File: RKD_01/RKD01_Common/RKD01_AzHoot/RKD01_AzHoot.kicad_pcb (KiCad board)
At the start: 2 copper layers, 19.1 x 28.6 mm, 3 parts, among them M1 Mark, P1 pointing

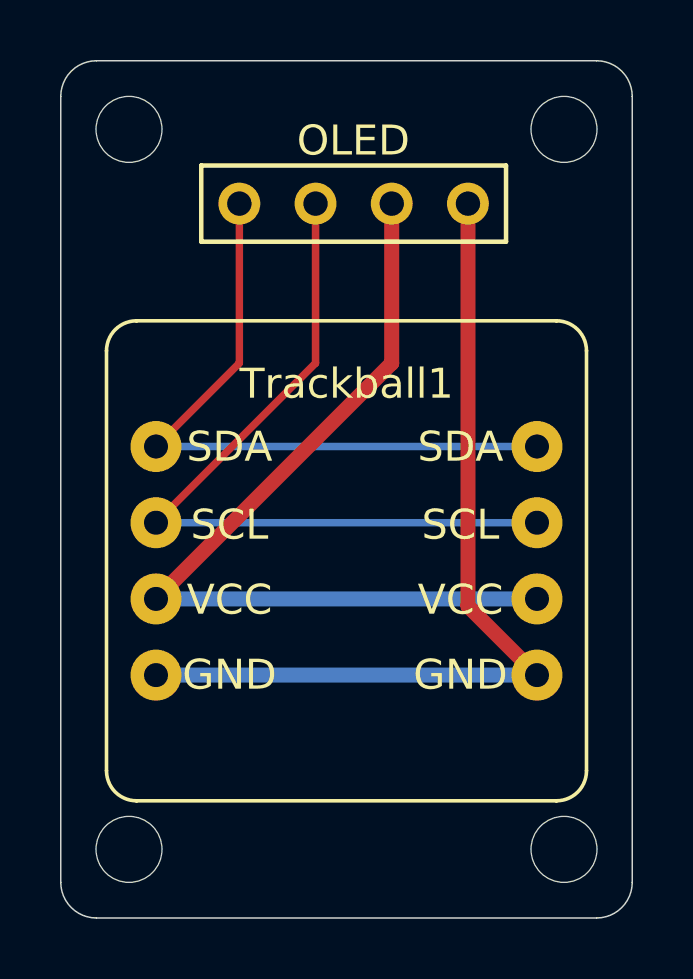
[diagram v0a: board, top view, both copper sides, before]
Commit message: 足場をカットに更新
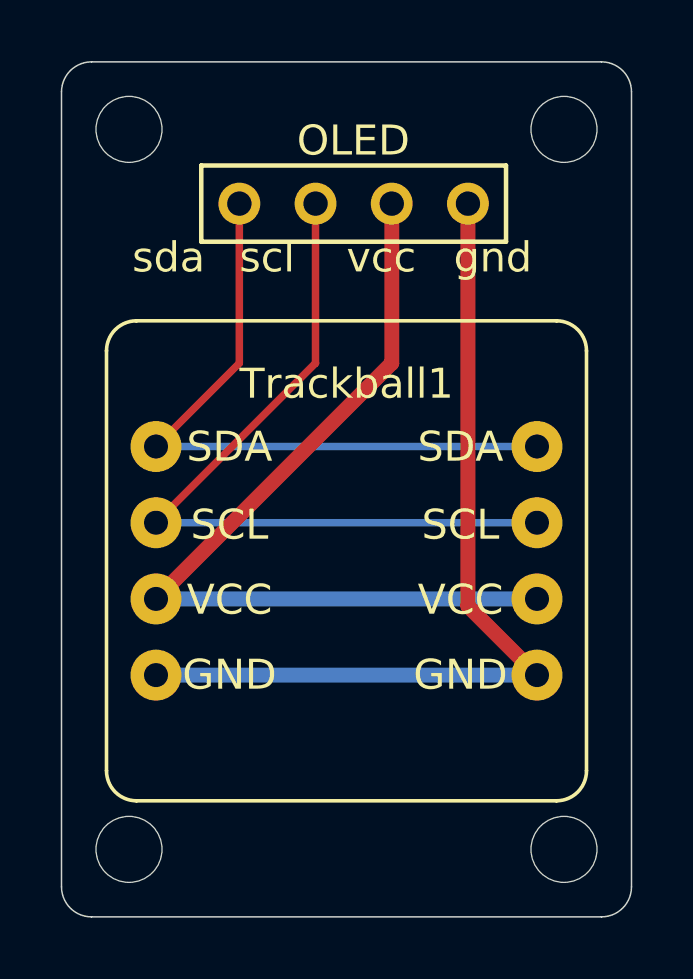
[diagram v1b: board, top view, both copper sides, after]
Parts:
- M1: footprint Rikkodo_FootPrint:rkd_Point_Hall -> Rikkodo_FootPrint:rkd_Point_Cut
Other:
- board size 19.1 x 28.6 mm -> 19 x 28.5 mm
- board text added: "gnd"
- board text added: "scl"
- board text added: "sda"
- board text added: "vcc"
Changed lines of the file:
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@@
 	(footprint "kicad:AZ1UBALL"
 		(layer "F.Cu")
-		(at 30.9563 103.5844)
+		(at 30.95625 103.584375)
 		(descr "Through hole straight pin header, 1x04, 2.54mm pitch, single row")
 		(tags "Through hole pin header THT 1x04 2.54mm single row")
@@
 		)
 		(sheetname "ルート")
-		(sheetfile "RKD01AzHoot.kicad_sch")
+		(sheetfile "RKD01_AzHoot.kicad_sch")
 		(attr through_hole)
 		(fp_line
@@
 		)
 		(sheetname "ルート")
-		(sheetfile "RKD01AzHoot.kicad_sch")
+		(sheetfile "RKD01_AzHoot.kicad_sch")
 		(attr through_hole)
 		(fp_line
@@
 		)
 	)
-	(footprint "Rikkodo_FootPrint:rkd_Point_Hall"
+	(footprint "Rikkodo_FootPrint:rkd_Point_Cut"
 		(layer "F.Cu")
-		(at 30.9563 101.2031)
+		(at 30.95625 101.203125)
 		(property "Reference" "M1"
 			(at 7 8.1 0)
@@
 			)
 		)
-		(property "Footprint" "Rikkodo_FootPrint:rkd_Point_Hall"
+		(property "Footprint" "Rikkodo_FootPrint:rkd_Point_Cut"
 			(at 0 0 0)
 			(layer "F.Fab")
@@
 		)
 		(sheetname "ルート")
-		(sheetfile "RKD01AzHoot.kicad_sch")
+		(sheetfile "RKD01_AzHoot.kicad_sch")
 		(attr through_hole)
 		(fp_line
@@
 			(layer "Cmts.User")
 		)
+		(fp_line
+			(start -9.5 -13.25)
+			(end -9.5 13.25)
+			(stroke
+				(width 0.05)
+				(type default)
+			)
+			(layer "Edge.Cuts")
+		)
+		(fp_line
+			(start -8.5 -14.25)
+			(end 8.5 -14.25)
+			(stroke
+				(width 0.05)
+				(type default)
+			)
+			(layer "Edge.Cuts")
+		)
+		(fp_line
+			(start 8.5 14.25)
+			(end -8.5 14.25)
+			(stroke
+				(width 0.05)
+				(type default)
+			)
+			(layer "Edge.Cuts")
+		)
+		(fp_line
+			(start 9.5 -13.25)
+			(end 9.5 13.25)
+			(stroke
+				(width 0.05)
+				(type default)
+			)
+			(layer "Edge.Cuts")
+		)
+		(fp_arc
+			(start -9.5 -13.25)
+			(mid -9.207107 -13.957107)
+			(end -8.5 -14.25)
+			(stroke
+				(width 0.05)
+				(type default)
+			)
+			(layer "Edge.Cuts")
+		)
+		(fp_arc
+			(start -8.5 14.25)
+			(mid -9.207107 13.957107)
+			(end -9.5 13.25)
+			(stroke
+				(width 0.05)
+				(type default)
+			)
+			(layer "Edge.Cuts")
+		)
+		(fp_arc
+			(start 8.5 -14.25)
+			(mid 9.207107 -13.957107)
+			(end 9.5 -13.25)
+			(stroke
+				(width 0.05)
+				(type default)
+			)
+			(layer "Edge.Cuts")
+		)
+		(fp_arc
+			(start 9.5 13.25)
+			(mid 9.207107 13.957107)
+			(end 8.5 14.25)
+			(stroke
+				(width 0.05)
+				(type default)
+			)
+			(layer "Edge.Cuts")
+		)
 		(fp_circle
 			(center -7.25 -12)
@@
 			(fill none)
 			(layer "F.CrtYd")
-		)
-		(fp_rect
-			(start -9.5 -14.25)
-			(end 9.5 14.25)
-			(stroke
-				(width 0.1)
-				(type default)
-			)
-			(fill none)
-			(layer "F.Fab")
 		)
 		(fp_rect
@@
 		)
 	)
-	(gr_line
-		(start 39.290625 115.490625)
-		(end 22.621875 115.490625)
-		(stroke
-			(width 0.05)
-			(type default)
-		)
-		(layer "Edge.Cuts")
-	)
-	(gr_arc
-		(start 21.43125 88.10625)
-		(mid 21.779976 87.264351)
-		(end 22.621875 86.915625)
-		(stroke
-			(width 0.05)
-			(type default)
-		)
-		(layer "Edge.Cuts")
-	)
-	(gr_line
-		(start 22.621875 86.915625)
-		(end 39.290625 86.915625)
-		(stroke
-			(width 0.05)
-			(type default)
-		)
-		(layer "Edge.Cuts")
-	)
-	(gr_arc
-		(start 40.48125 114.3)
-		(mid 40.132524 115.141899)
-		(end 39.290625 115.490625)
-		(stroke
-			(width 0.05)
-			(type default)
-		)
-		(layer "Edge.Cuts")
-	)
-	(gr_arc
-		(start 22.621875 115.490625)
-		(mid 21.779976 115.141899)
-		(end 21.43125 114.3)
-		(stroke
-			(width 0.05)
-			(type default)
-		)
-		(layer "Edge.Cuts")
-	)
-	(gr_arc
-		(start 39.290625 86.915625)
-		(mid 40.132524 87.264351)
-		(end 40.48125 88.10625)
-		(stroke
-			(width 0.05)
-			(type default)
-		)
-		(layer "Edge.Cuts")
-	)
-	(gr_line
-		(start 40.48125 88.10625)
-		(end 40.48125 114.3)
-		(stroke
-			(width 0.05)
-			(type default)
-		)
-		(layer "Edge.Cuts")
-	)
-	(gr_line
-		(start 21.43125 114.3)
-		(end 21.43125 88.10625)
-		(stroke
-			(width 0.05)
-			(type default)
-		)
-		(layer "Edge.Cuts")
+	(gr_text "sda"
+		(at 26.19375 94.059375 0)
+		(layer "B.SilkS")
+		(effects
+			(font
+				(size 1 1)
+				(thickness 0.15)
+			)
+			(justify left bottom mirror)
+		)
+	)
+	(gr_text "scl"
+		(at 29.765625 94.059375 0)
+		(layer "B.SilkS")
+		(effects
+			(font
+				(size 1 1)
+				(thickness 0.15)
+			)
+			(justify left bottom mirror)
+		)
+	)
+	(gr_text "gnd"
+		(at 36.909375 94.059375 0)
+		(layer "B.SilkS")
+		(effects
+			(font
+				(size 1 1)
+				(thickness 0.15)
+			)
+			(justify left bottom mirror)
+		)
+	)
+	(gr_text "vcc"
+		(at 33.3375 94.059375 0)
+		(layer "B.SilkS")
+		(effects
+			(font
+				(size 1 1)
+				(thickness 0.15)
+			)
+			(justify left bottom mirror)
+		)
+	)
+	(gr_text "scl"
+		(at 27.384375 94.059375 0)
+		(layer "F.SilkS")
+		(effects
+			(font
+				(size 1 1)
+				(thickness 0.15)
+			)
+			(justify left bottom)
+		)
+	)
+	(gr_text "sda"
+		(at 23.8125 94.059375 0)
+		(layer "F.SilkS")
+		(effects
+			(font
+				(size 1 1)
+				(thickness 0.15)
+			)
+			(justify left bottom)
+		)
+	)
+	(gr_text "gnd"
+		(at 34.528125 94.059375 0)
+		(layer "F.SilkS")
+		(effects
+			(font
+				(size 1 1)
+				(thickness 0.15)
+			)
+			(justify left bottom)
+		)
+	)
+	(gr_text "vcc"
+		(at 30.95625 94.059375 0)
+		(layer "F.SilkS")
+		(effects
+			(font
+				(size 1 1)
+				(thickness 0.15)
+			)
+			(justify left bottom)
+		)
 	)
 	(segment
